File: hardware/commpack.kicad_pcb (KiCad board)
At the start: 2 copper layers, 103.8 x 62.5 mm, 14 parts, among them J1 1240COMM, J2 1240COMM_EXT, J3 L8BE-1G1T-91A, J4 USB_B

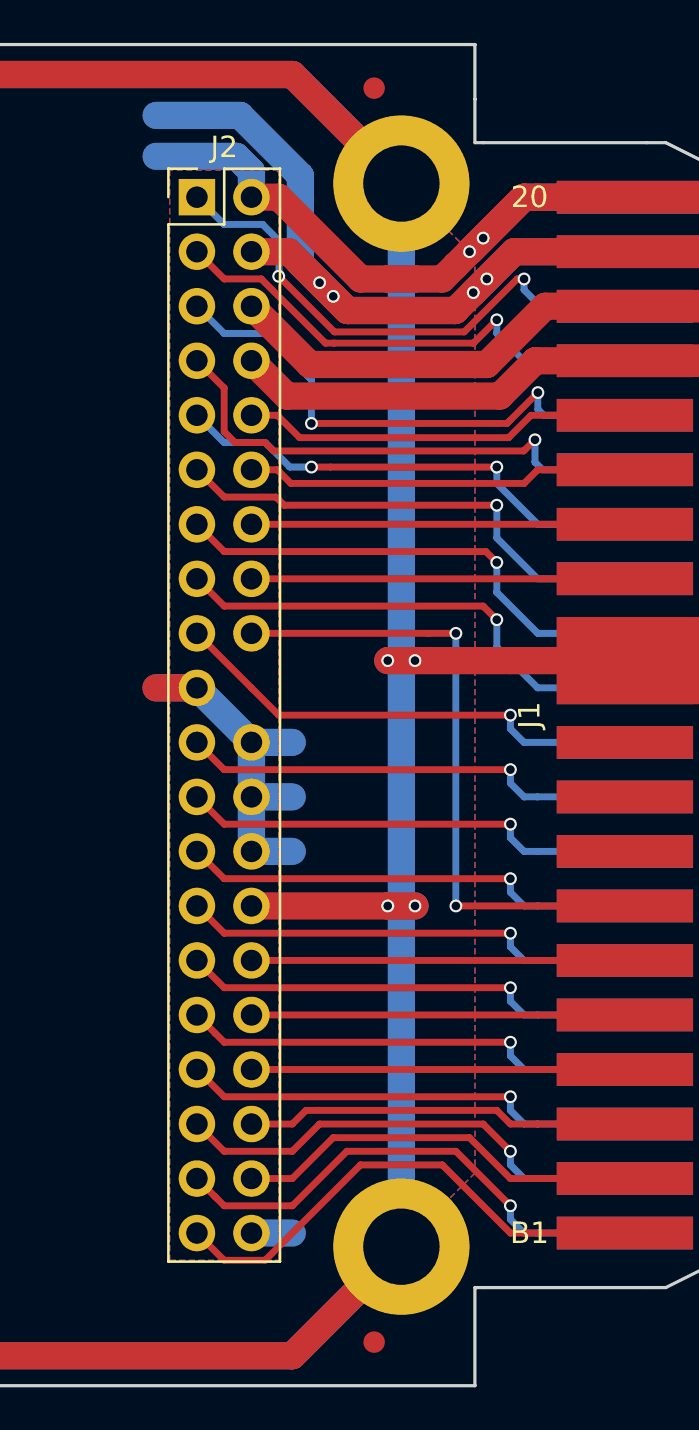
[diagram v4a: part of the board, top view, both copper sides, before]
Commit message: Add ground pour over card-edge connector.
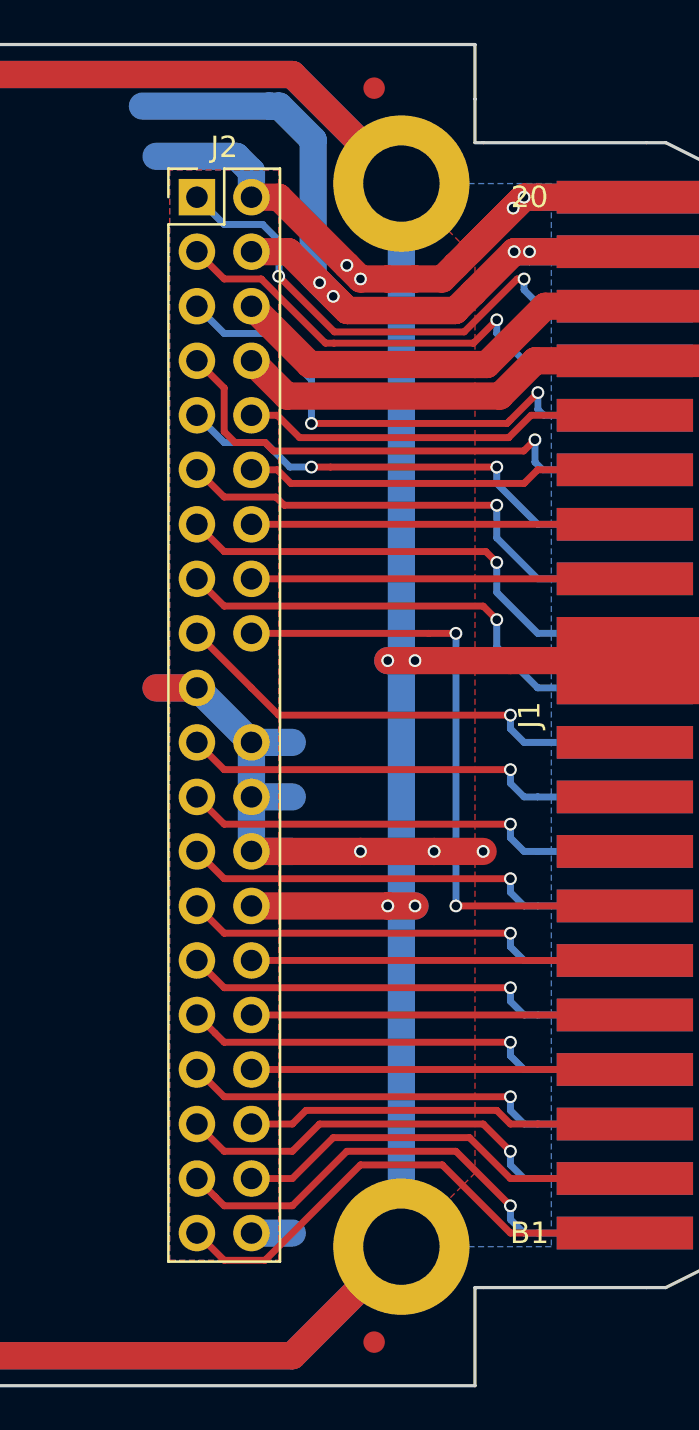
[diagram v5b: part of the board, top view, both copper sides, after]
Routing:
- net GND: track 52.1 -> 60.1 mm, vias 2 -> 7
- net +5V: track 41.3 -> 40.7 mm

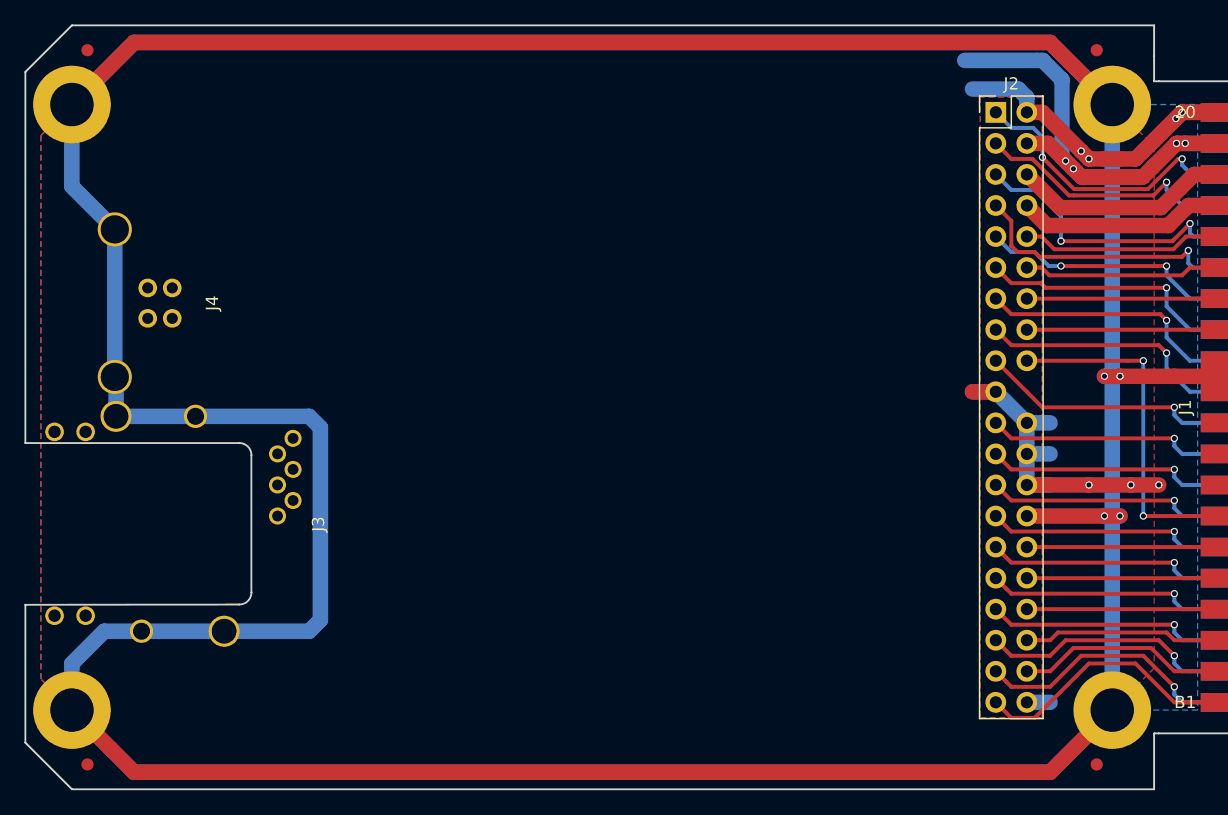
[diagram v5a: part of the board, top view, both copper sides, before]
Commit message: Add 27128 socket to PCB and route it.
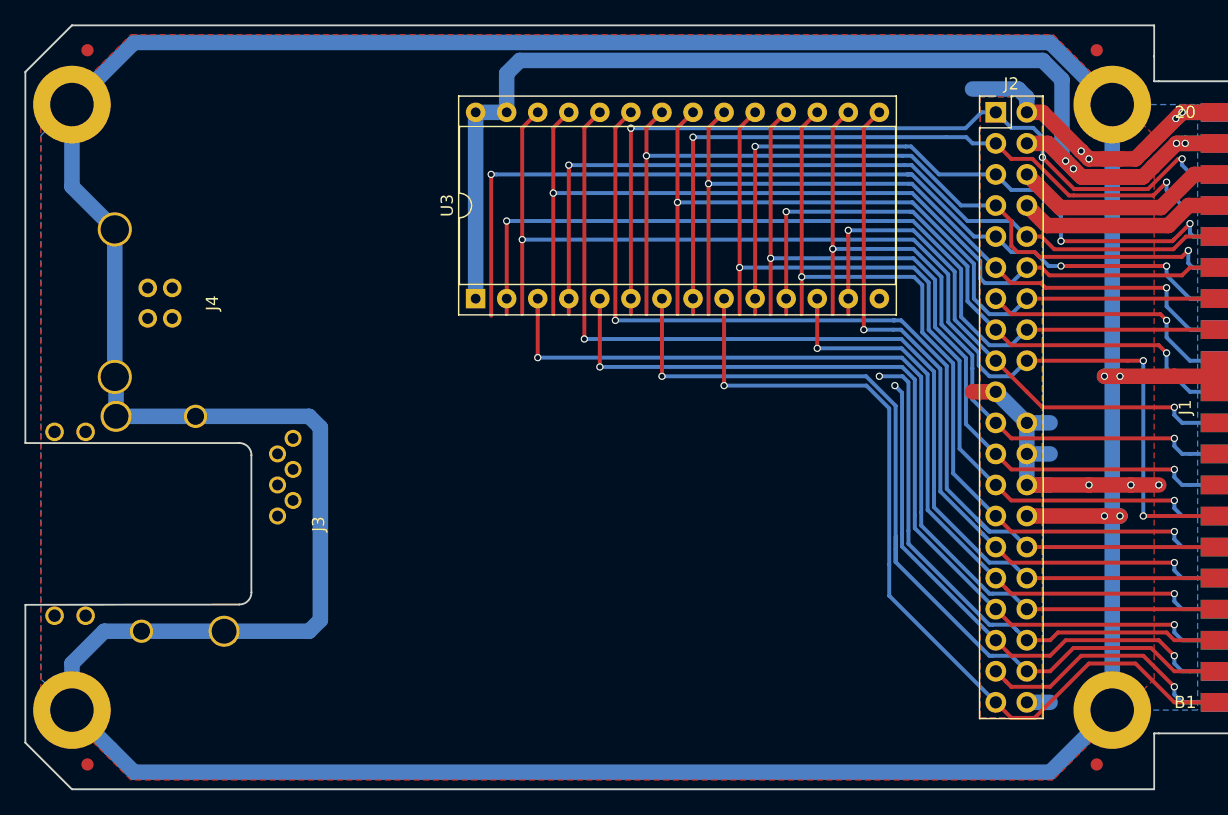
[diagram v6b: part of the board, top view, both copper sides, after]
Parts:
- added U3: 27C128, Housings_DIP:DIP-28_W15.24mm_Socket, F.Cu at (158.8, 80.0)
- moved Bonsai 7.36 mm to (186.8, 88.8)
- moved G*** 6.81 mm to (173.1, 87.9)
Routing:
- net Earth_Protective: track 510.8 -> 332.2 mm
- net /H-A9: track 14.2 -> 84.1 mm, vias 0 -> 1
- net /H-A11: track 14.2 -> 81.9 mm, vias 0 -> 1
- net /H-A13: track 26.9 -> 93.3 mm, vias 2 -> 3
- net /H-A7: track 14.2 -> 76.0 mm, vias 0 -> 1
- net /H-A8: track 14.8 -> 74.9 mm, vias 0 -> 1
- net +5V: track 40.7 -> 99.6 mm
- net /H-A12: track 14.2 -> 72.2 mm, vias 0 -> 1
- net /H-A3: track 15.8 -> 72.9 mm, vias 0 -> 1
- net /H-INT: track 19.4 -> 74.6 mm, vias 2 -> 3
- net /H-A5: track 18.2 -> 72.8 mm, vias 1 -> 2
- net /H-A6: track 15.1 -> 67.2 mm, vias 0 -> 1
- net /H-D7: track 18.2 -> 70.0 mm, vias 1 -> 2
- net /H-A10: track 14.2 -> 65.8 mm, vias 0 -> 1
- net /H-A1: track 20.4 -> 70.8 mm, vias 0 -> 1
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
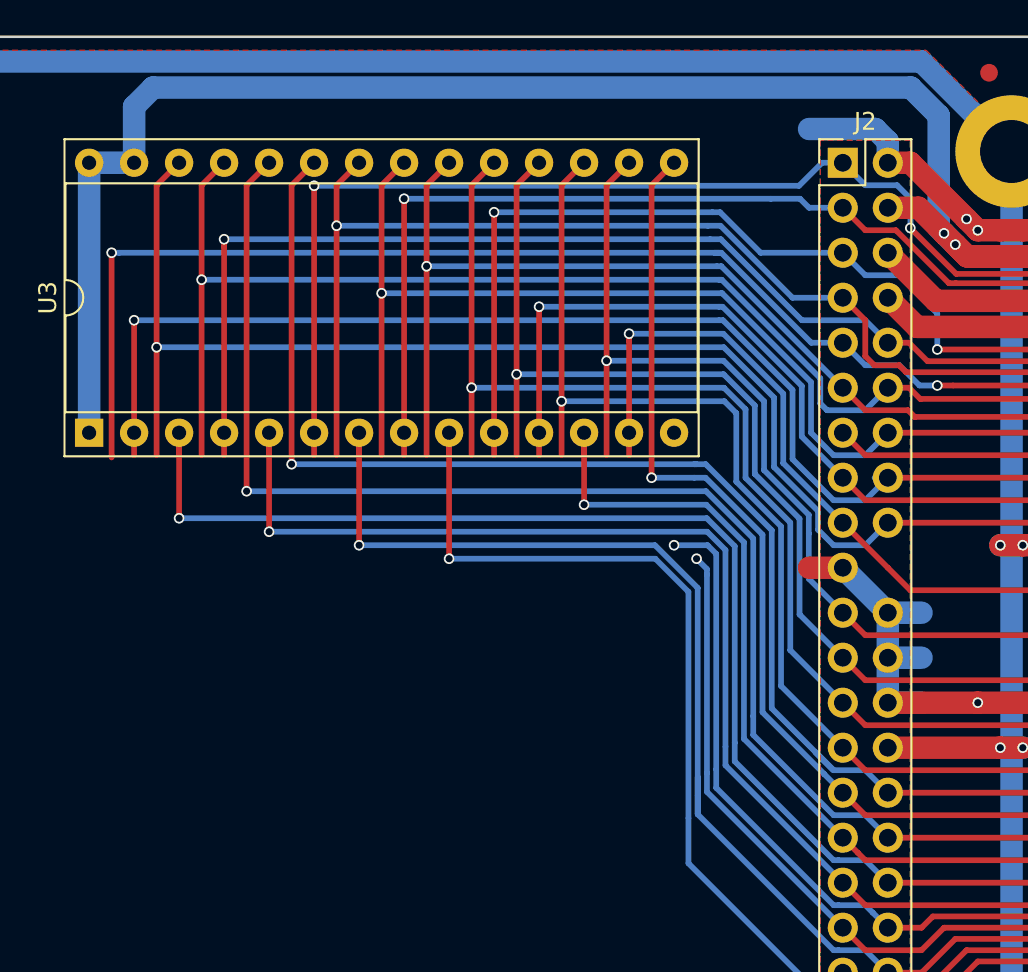
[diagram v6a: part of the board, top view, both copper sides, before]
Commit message: Make routing for ROM socket more compact.
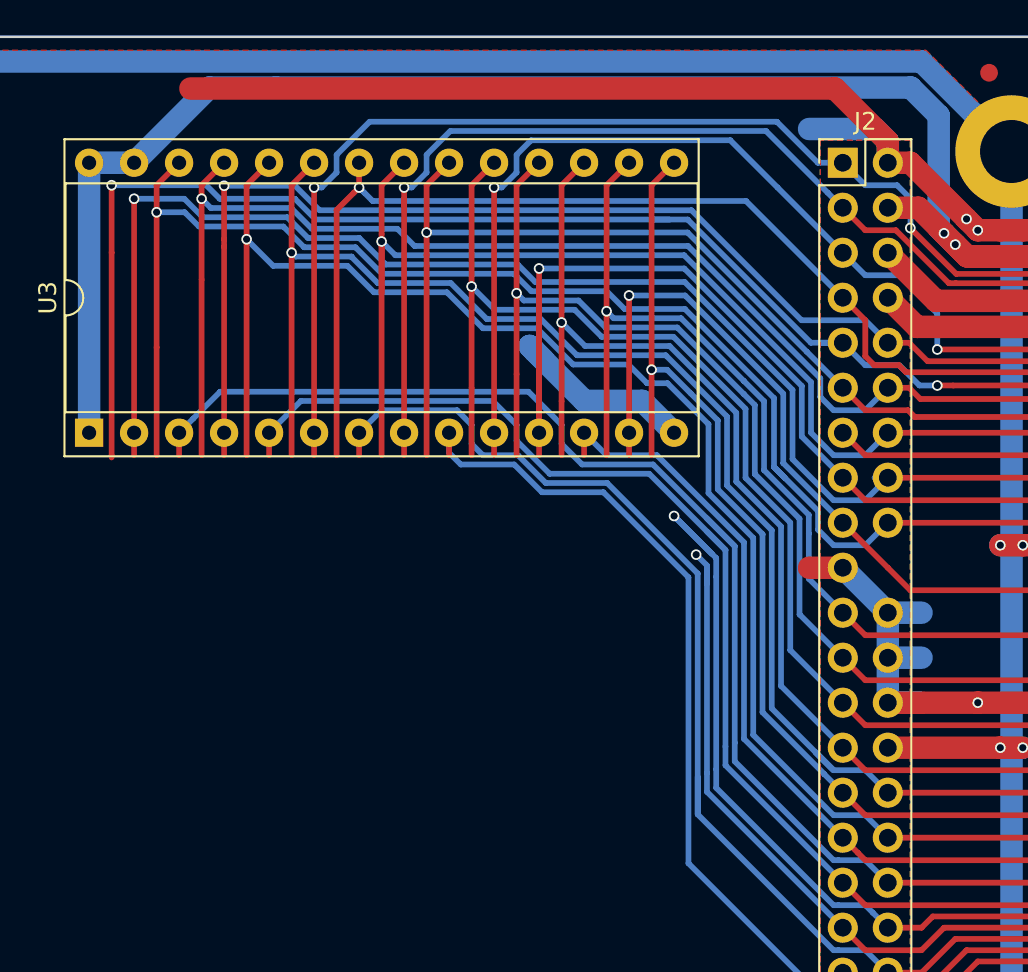
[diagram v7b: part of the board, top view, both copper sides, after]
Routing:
- net GND: track 58.1 -> 111.3 mm
- net /H-D0: track 50.8 -> 62.1 mm
- net /H-A12: track 72.2 -> 81.9 mm
- net /H-INT: track 74.6 -> 81.9 mm
- net /H-A11: track 81.9 -> 88.5 mm
- net /H-A9: track 84.1 -> 90.2 mm
- net /H-A0: track 56.2 -> 61.0 mm
- net /H-A2: track 59.6 -> 64.1 mm
- net /H-A6: track 67.2 -> 71.4 mm
- net /H-A10: track 65.8 -> 70.0 mm
- net /H-A13: track 93.3 -> 97.3 mm
- net /H-~CS: track 43.5 -> 47.1 mm
- net /H-D3: track 60.5 -> 64.1 mm
- net /H-D2: track 44.9 -> 47.9 mm
- net /H-A1: track 70.8 -> 67.7 mm, vias 1 -> 0
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
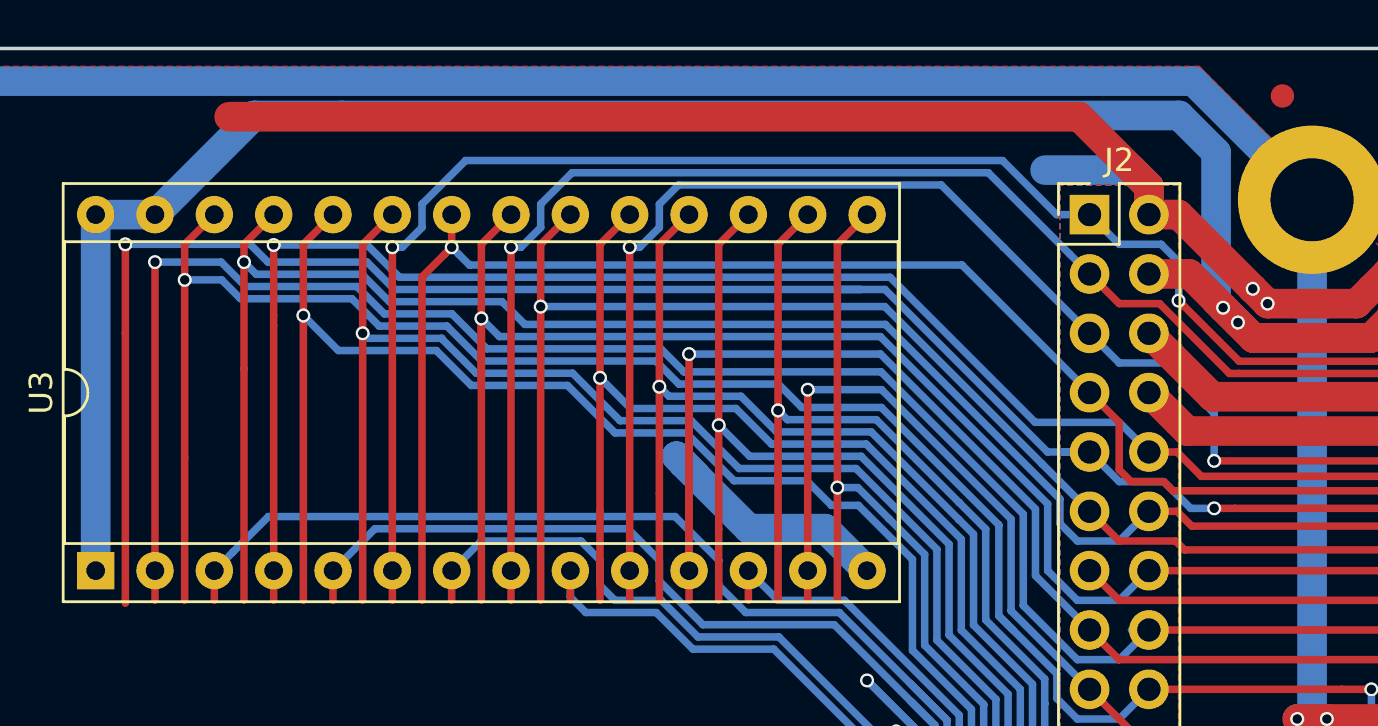
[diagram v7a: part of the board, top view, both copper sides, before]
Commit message: Duplicate trace cleanup on export.
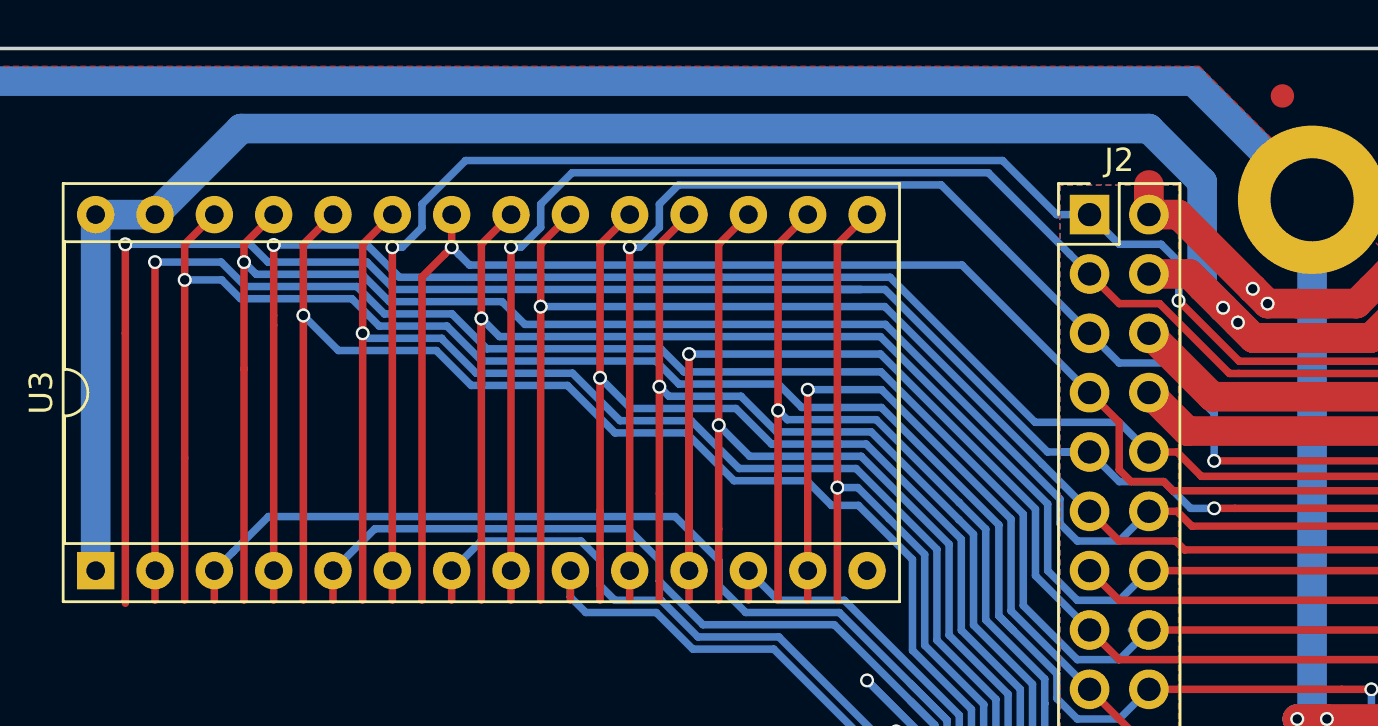
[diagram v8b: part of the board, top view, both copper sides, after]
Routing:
- net GND: track 111.3 -> 53.5 mm
- net +5V: track 97.7 -> 96.2 mm
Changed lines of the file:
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@@
     (links 80)
     (no_connects 0)
-    (area 121.844999 57.582999 225.754001 120.217001)
+    (area 115.514286 49.254999 230.399001 128.545001)
     (thickness 1.6)
     (drawings 66)
-    (tracks 674)
+    (tracks 662)
     (zones 0)
     (modules 15)
@@
     (pcbplotparams
       (layerselection 0x010f0_80000001)
-      (usegerberextensions false)
+      (usegerberextensions true)
       (excludeedgelayer true)
       (linewidth 0.100000)
@@
   (gr_line (start 225.679 113.03) (end 225.679 63.5) (angle 90) (layer Edge.Cuts) (width 0.15))
   (gr_line (start 222.25 62.23) (end 214.63 62.23) (angle 90) (layer Edge.Cuts) (width 0.15))
-  (segment (start 183.616506 75.11025) (end 184.404 75.897744) (width 1.27) (layer B.Cu) (net 1))
-  (segment (start 183.896 75.389745) (end 183.616506 75.11025) (width 1.27) (layer B.Cu) (net 1))
-  (segment (start 186.704678 78.2123) (end 183.896 75.403622) (width 1.27) (layer B.Cu) (net 1))
-  (segment (start 183.896 75.403622) (end 183.896 75.389745) (width 1.27) (layer B.Cu) (net 1))
-  (segment (start 191.77 80.01) (end 189.9723 78.2123) (width 1.27) (layer B.Cu) (net 1))
-  (segment (start 189.9723 78.2123) (end 186.704678 78.2123) (width 1.27) (layer B.Cu) (net 1))
-  (segment (start 200.846081 60.579) (end 164.465 60.579) (width 1.27) (layer F.Cu) (net 1))
-  (segment (start 203.835 64.77) (end 203.835 63.567919) (width 1.27) (layer F.Cu) (net 1))
-  (segment (start 203.835 63.567919) (end 200.846081 60.579) (width 1.27) (layer F.Cu) (net 1))
+  (segment (start 203.835 64.77) (end 203.835 63.5) (width 1.27) (layer F.Cu) (net 1))
   (segment (start 208.915 68.58) (end 208.28 67.945) (width 1.27) (layer F.Cu) (net 1))
   (segment (start 208.28 67.945) (end 205.105 64.77) (width 1.27) (layer F.Cu) (net 1))
@@
   (segment (start 203.835 90.17) (end 203.835 95.25) (width 1.27) (layer B.Cu) (net 1))
   (segment (start 201.295 87.63) (end 203.835 90.17) (width 1.27) (layer B.Cu) (net 1))
-  (segment (start 203.132081 62.865) (end 199.39 62.865) (width 1.27) (layer B.Cu) (net 1))
-  (segment (start 203.835 64.77) (end 203.835 63.567919) (width 1.27) (layer B.Cu) (net 1))
-  (segment (start 203.835 63.567919) (end 203.132081 62.865) (width 1.27) (layer B.Cu) (net 1))
   (segment (start 203.835 64.77) (end 205.105 64.77) (width 1.27) (layer F.Cu) (net 1))
   (segment (start 217.17 64.77) (end 218.059 64.77) (width 1.27) (layer F.Cu) (net 1))
@@
   (segment (start 216.535 64.77) (end 213.36 67.945) (width 1.27) (layer F.Cu) (net 1))
   (segment (start 213.36 67.945) (end 212.725 68.58) (width 1.27) (layer F.Cu) (net 1))
-  (segment (start 165.53499 60.52501) (end 161.29 64.77) (width 1.27) (layer B.Cu) (net 2))
-  (segment (start 205.131102 60.52501) (end 169.291 60.52501) (width 1.27) (layer B.Cu) (net 2))
-  (segment (start 169.291 60.52501) (end 165.53499 60.52501) (width 1.27) (layer B.Cu) (net 2))
+  (segment (start 207.01 68.753908) (end 206.113479 67.857387) (width 1.27) (layer B.Cu) (net 2))
+  (segment (start 206.113479 67.857387) (end 206.113479 63.365479) (width 1.27) (layer B.Cu) (net 2))
+  (segment (start 206.113479 63.365479) (end 203.835 61.087) (width 1.27) (layer B.Cu) (net 2))
+  (segment (start 203.835 61.087) (end 164.973 61.087) (width 1.27) (layer B.Cu) (net 2))
+  (segment (start 164.973 61.087) (end 161.29 64.77) (width 1.27) (layer B.Cu) (net 2))
   (segment (start 158.75 64.77) (end 158.75 80.01) (width 1.27) (layer B.Cu) (net 2))
   (segment (start 158.75 64.77) (end 161.29 64.77) (width 1.27) (layer B.Cu) (net 2))
-  (segment (start 207.01 68.753908) (end 206.710001 68.453909) (width 1.27) (layer B.Cu) (net 2))
-  (segment (start 206.710001 68.453909) (end 206.710001 62.103909) (width 1.27) (layer B.Cu) (net 2))
-  (segment (start 206.710001 62.103909) (end 205.131102 60.52501) (width 1.27) (layer B.Cu) (net 2))
   (segment (start 218.059 67.31) (end 216.789 67.31) (width 1.27) (layer B.Cu) (net 2))
   (segment (start 216.789 67.31) (end 216.073908 67.31) (width 1.27) (layer B.Cu) (net 2))
